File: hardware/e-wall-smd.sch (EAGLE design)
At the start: 45 parts, among them IC1 74HCT595D, IC2 74HCT595D, IC3 74HCT595D, Q1 2N7002P, Q10 2N7002P, Q11 2N7002P, Q12 2N7002P, Q13 2N7002P, Q14 2N7002P, Q15 2N7002P, Q16 2N7002P, Q17 2N7002P, Q18 2N7002P, Q19 2N7002P, Q2 2N7002P, Q20 2N7002P, Q21 2N7002P, Q22 2N7002P, Q23 2N7002P, Q24 2N7002P, Q3 2N7002P, Q4 2N7002P, Q5 2N7002P, Q6 2N7002P, Q7 2N7002P, Q8 2N7002P, Q9 2N7002P, T1 BC547, T2 BC557, T3 BC547

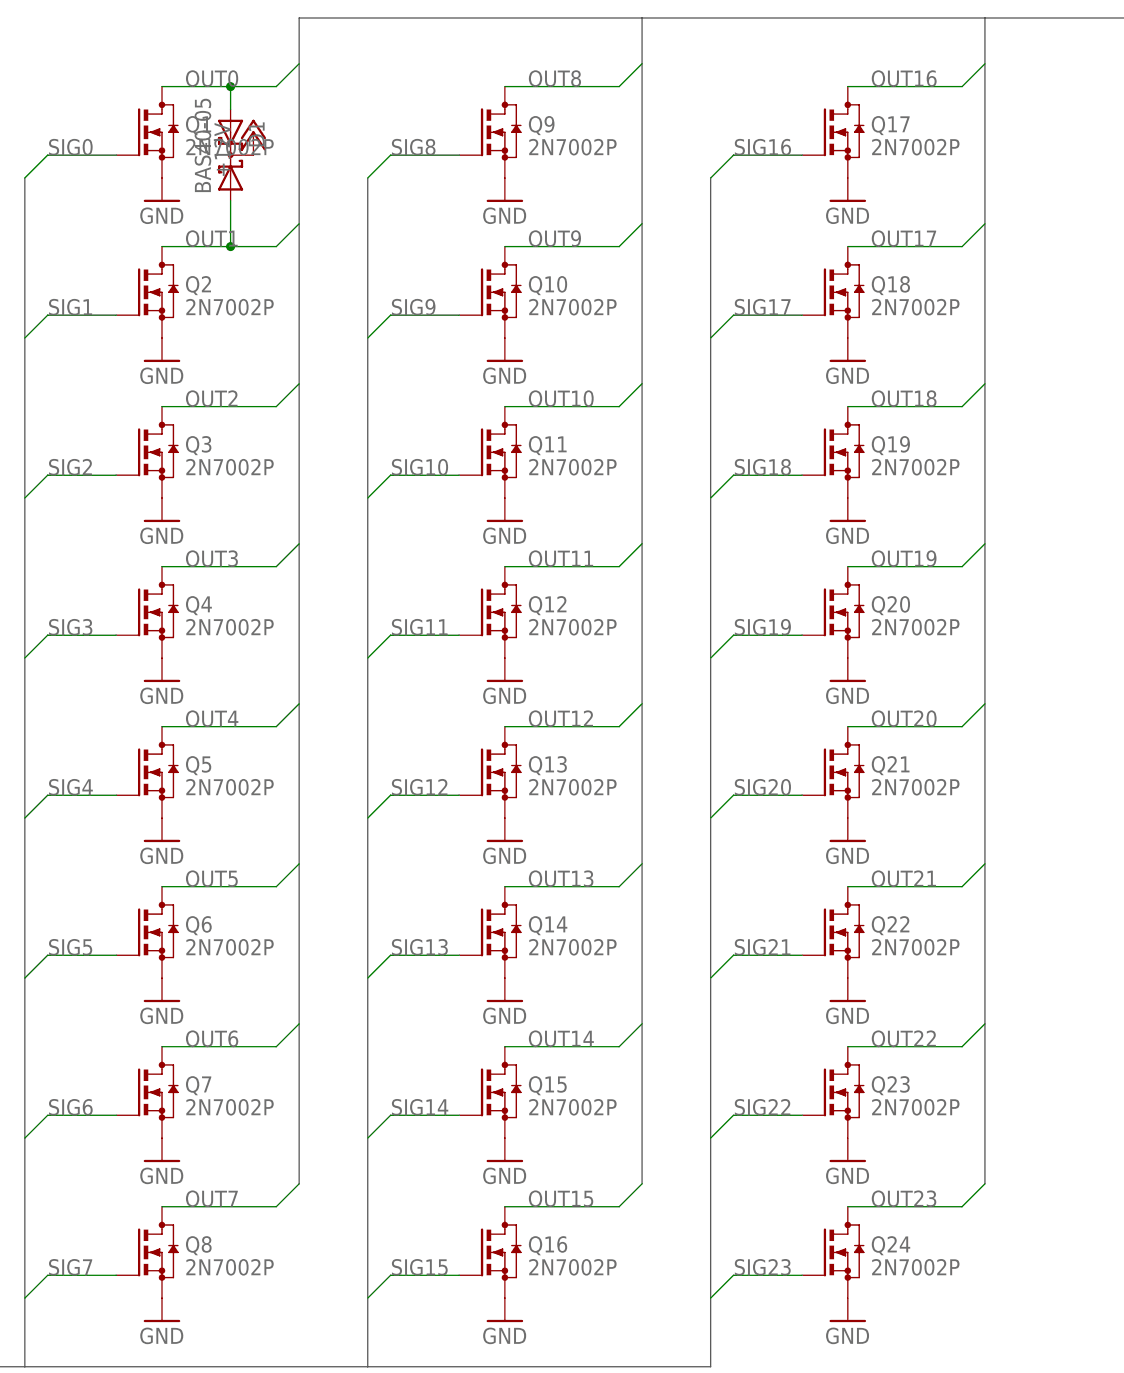
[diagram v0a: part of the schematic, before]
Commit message: Freilaufdiode ergänzt
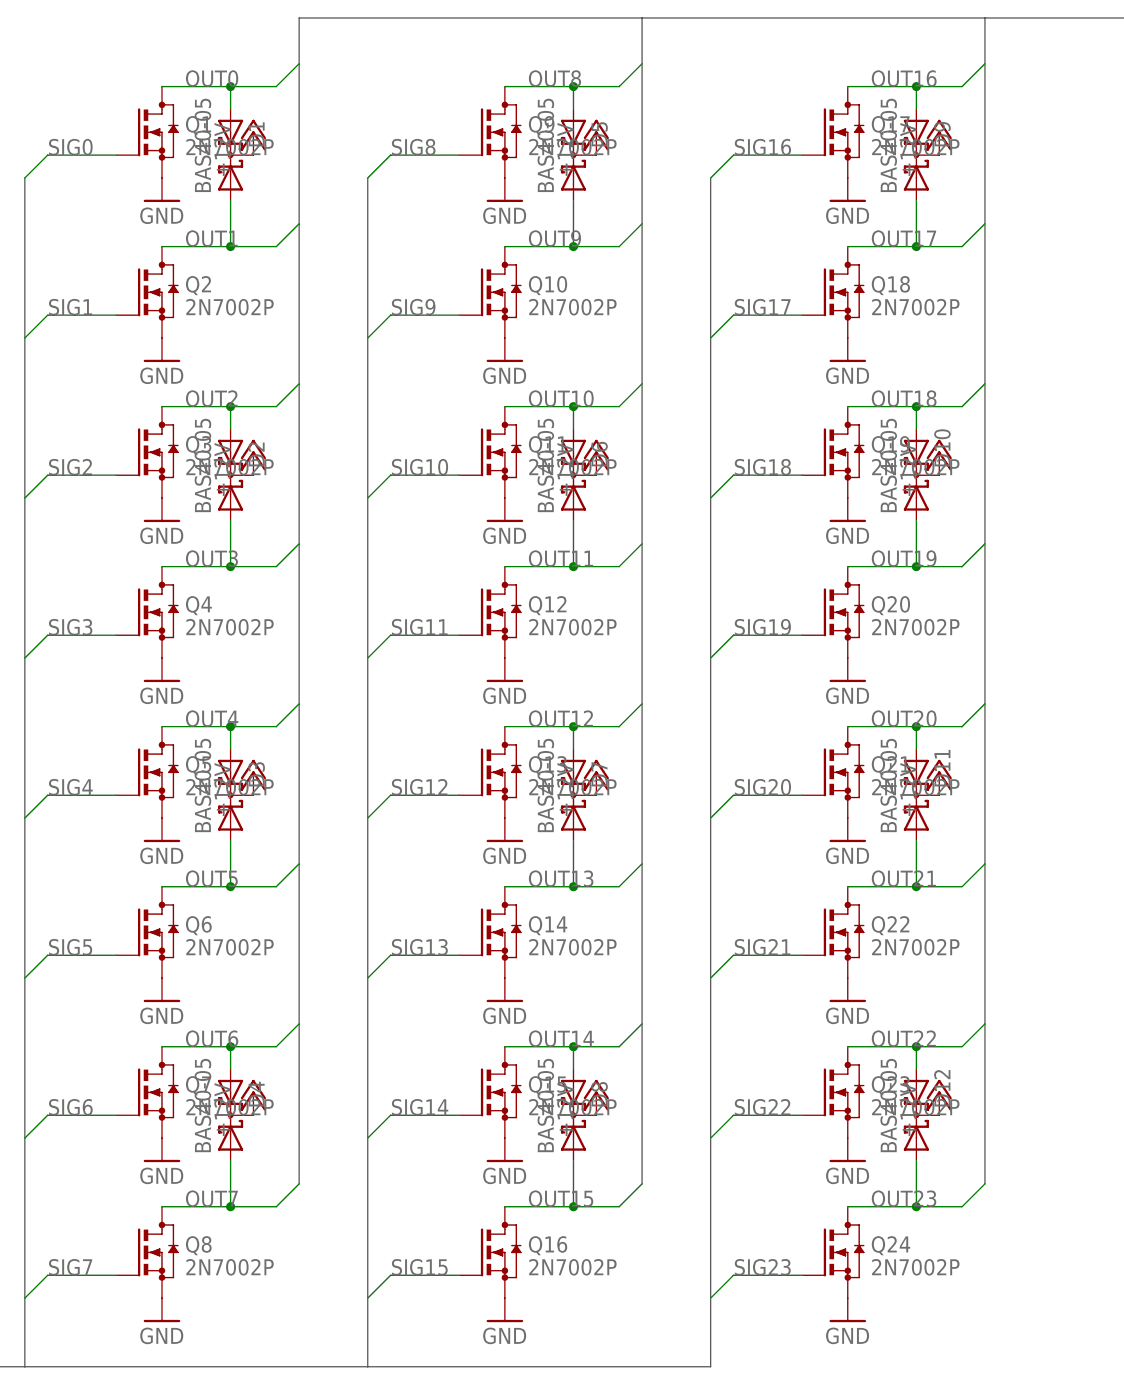
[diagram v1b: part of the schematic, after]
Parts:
- added D10, D11, D12, D2, D3, D4, D5, D6, D7, D8, D9: BAS40-05, diode:BAS40-05
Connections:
- net +12V: now also D10.C, D11.C, D12.C, D2.C, D3.C, D4.C, D5.C, D6.C, D7.C, D8.C, D9.C
- net OUT10: now also D6.A2
- net OUT11: now also D6.A1
- net OUT12: now also D7.A2
- net OUT13: now also D7.A1
- net OUT14: now also D8.A2
- net OUT15: now also D8.A1
- net OUT16: now also D9.A2
- net OUT17: now also D9.A1
- net OUT18: now also D10.A2
- net OUT19: now also D10.A1
- net OUT2: now also D2.A2
- net OUT20: now also D11.A2
- net OUT21: now also D11.A1
- net OUT22: now also D12.A2
- net OUT23: now also D12.A1
- net OUT3: now also D2.A1
- net OUT4: now also D3.A2
- net OUT5: now also D3.A1
- net OUT6: now also D4.A2
- net OUT7: now also D4.A1
- net OUT8: now also D5.A2
- net OUT9: now also D5.A1

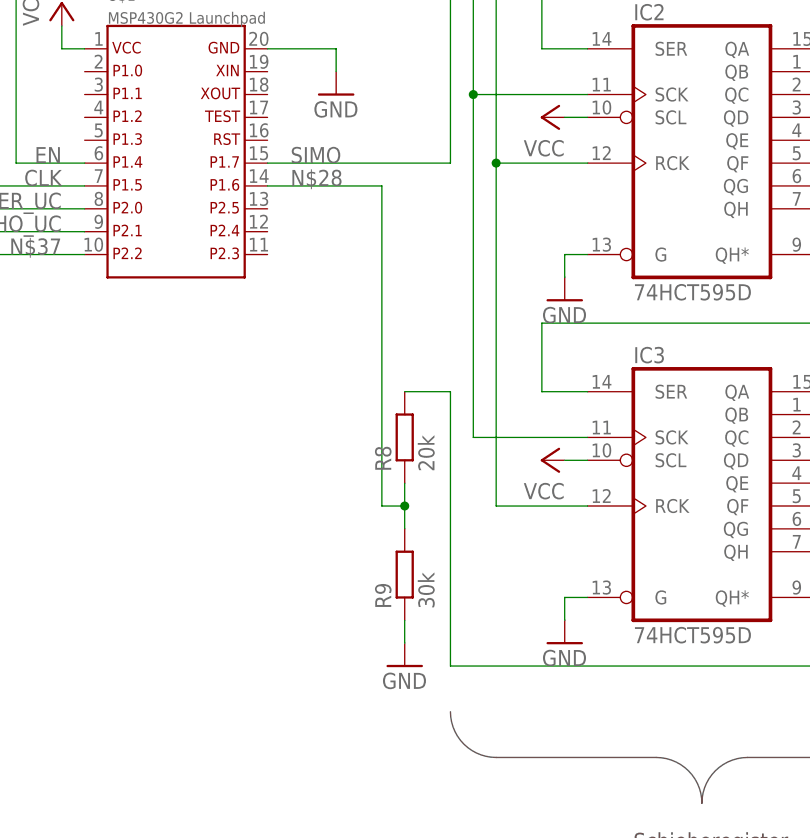
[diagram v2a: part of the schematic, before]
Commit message: Leitungen für SPI umbenannt
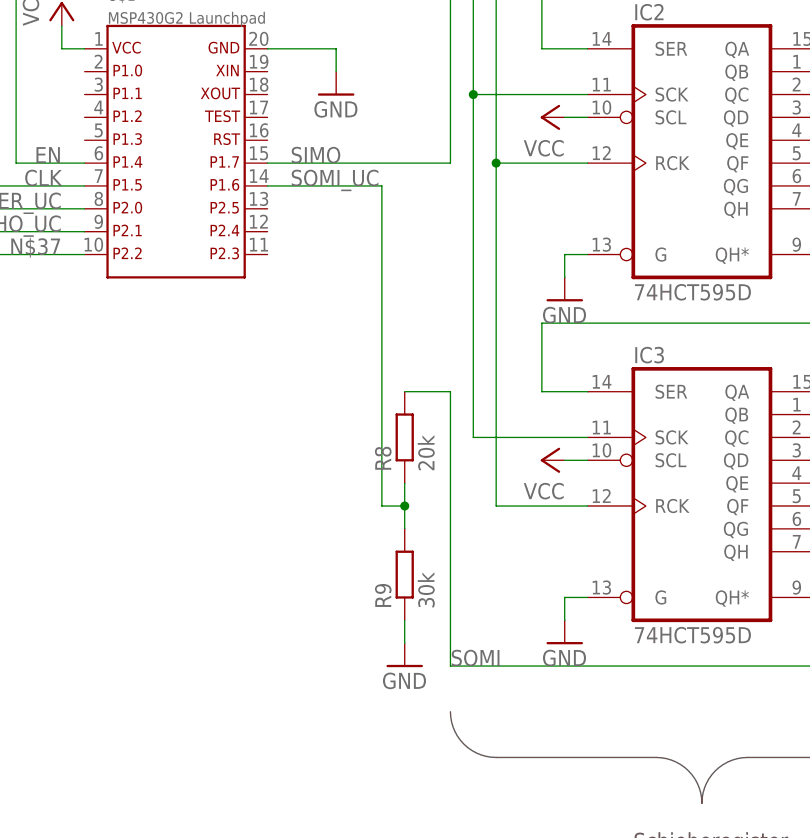
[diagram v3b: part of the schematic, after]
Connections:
- net N$28 renamed SOMI_UC
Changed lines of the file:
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@@
 <pinref part="R8" gate="G$1" pin="2"/>
 <wire x1="104.14" y1="35.56" x2="109.22" y2="35.56" width="0.1524" layer="91"/>
+<label x="109.22" y="5.08" size="1.778" layer="95"/>
 </segment>
 </net>
@@
 </segment>
 </net>
-<net name="N$28" class="0">
+<net name="SOMI_UC" class="0">
 <segment>
 <wire x1="101.6" y1="58.42" x2="88.9" y2="58.42" width="0.1524" layer="91"/>

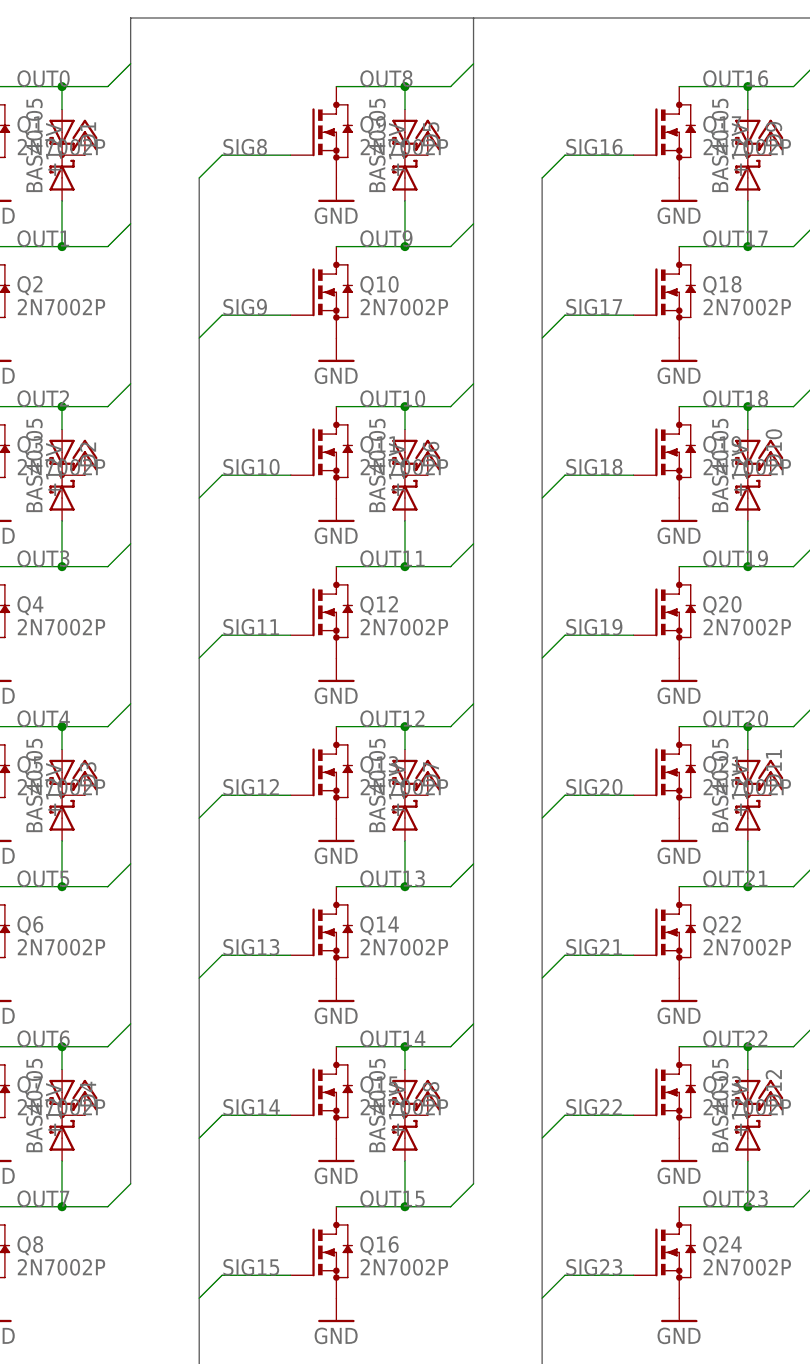
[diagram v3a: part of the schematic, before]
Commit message: Schieberegister verschoben
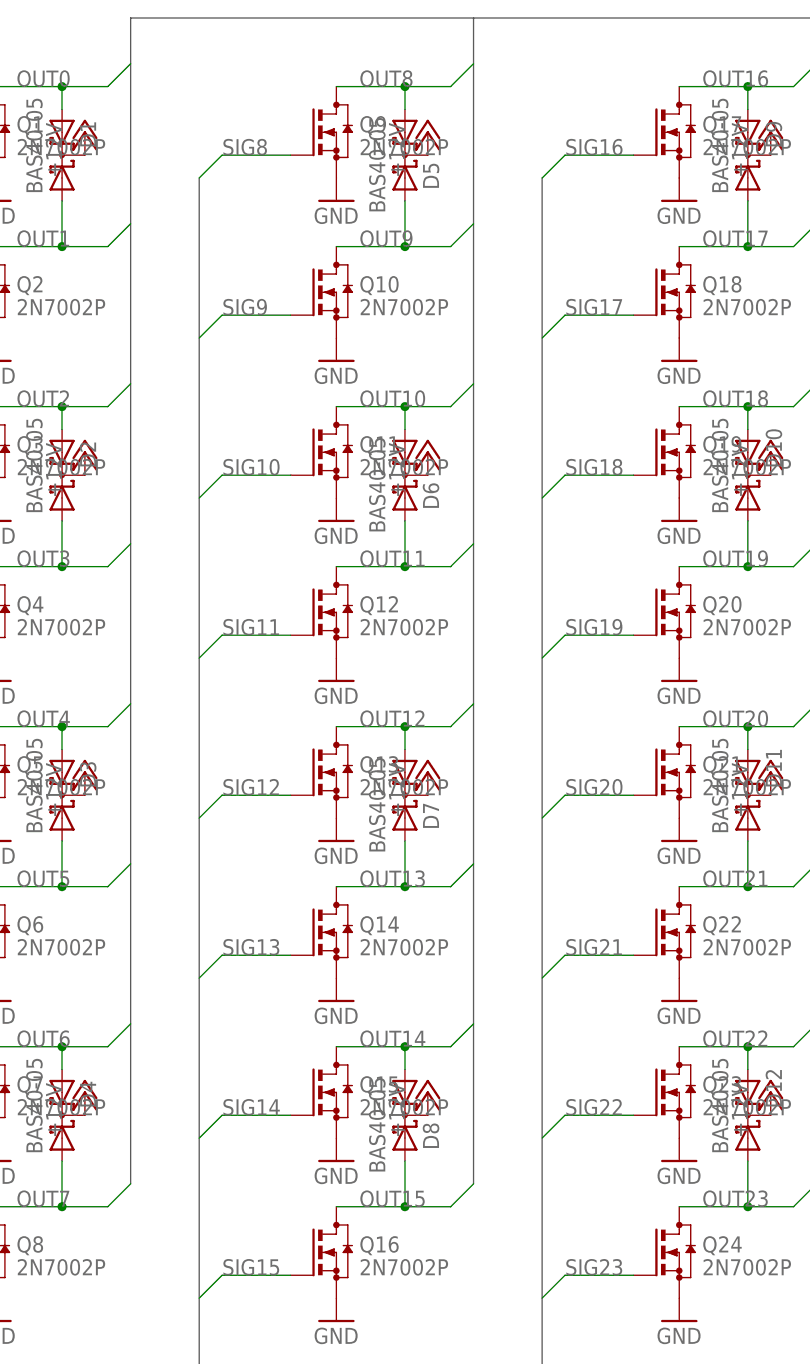
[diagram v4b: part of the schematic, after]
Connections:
- net OUT10: now also D6.A1; no longer D6.A2
- net OUT11: now also D6.A2; no longer D6.A1
- net OUT12: now also D7.A1; no longer D7.A2
- net OUT13: now also D7.A2; no longer D7.A1
- net OUT14: now also D8.A1; no longer D8.A2
- net OUT15: now also D8.A2; no longer D8.A1
- net OUT8: now also D5.A1; no longer D5.A2
- net OUT9: now also D5.A2; no longer D5.A1
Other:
- moved on the sheet: D5, D6, D7, D8
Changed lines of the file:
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@@
 <instance part="D3" gate="G$1" x="195.58" y="68.58" rot="MR90"/>
 <instance part="D4" gate="G$1" x="195.58" y="33.02" rot="MR90"/>
-<instance part="D5" gate="G$1" x="233.68" y="139.7" rot="MR90"/>
-<instance part="D6" gate="G$1" x="233.68" y="104.14" rot="MR90"/>
-<instance part="D7" gate="G$1" x="233.68" y="68.58" rot="MR90"/>
-<instance part="D8" gate="G$1" x="233.68" y="33.02" rot="MR90"/>
+<instance part="D5" gate="G$1" x="233.68" y="139.7" rot="R270"/>
+<instance part="D6" gate="G$1" x="233.68" y="104.14" rot="R270"/>
+<instance part="D7" gate="G$1" x="233.68" y="68.58" rot="R270"/>
+<instance part="D8" gate="G$1" x="233.68" y="33.02" rot="R270"/>
 <instance part="D9" gate="G$1" x="271.78" y="139.7" rot="MR90"/>
 <instance part="D10" gate="G$1" x="271.78" y="104.14" rot="MR90"/>
@@
 <wire x1="238.76" y1="147.32" x2="241.3" y2="149.86" width="0.1524" layer="91"/>
 <label x="228.6" y="147.32" size="1.778" layer="95"/>
-<pinref part="D5" gate="G$1" pin="A2"/>
+<pinref part="D5" gate="G$1" pin="A1"/>
 <wire x1="233.68" y1="144.78" x2="233.68" y2="147.32" width="0.1524" layer="91"/>
 <junction x="233.68" y="147.32"/>
@@
 <wire x1="238.76" y1="129.54" x2="241.3" y2="132.08" width="0.1524" layer="91"/>
 <label x="228.6" y="129.54" size="1.778" layer="95"/>
-<pinref part="D5" gate="G$1" pin="A1"/>
+<pinref part="D5" gate="G$1" pin="A2"/>
 <wire x1="233.68" y1="134.62" x2="233.68" y2="129.54" width="0.1524" layer="91"/>
 <junction x="233.68" y="129.54"/>
@@
 <wire x1="238.76" y1="111.76" x2="241.3" y2="114.3" width="0.1524" layer="91"/>
 <label x="228.6" y="111.76" size="1.778" layer="95"/>
-<pinref part="D6" gate="G$1" pin="A2"/>
-<wire x1="233.68" y1="109.22" x2="233.68" y2="111.76" width="0.1524" layer="91"/>
+<pinref part="D6" gate="G$1" pin="A1"/>
+<wire x1="233.68" y1="111.76" x2="233.68" y2="109.22" width="0.1524" layer="91"/>
 <junction x="233.68" y="111.76"/>
 </segment>
@@
 <wire x1="238.76" y1="93.98" x2="241.3" y2="96.52" width="0.1524" layer="91"/>
 <label x="228.6" y="93.98" size="1.778" layer="95"/>
-<pinref part="D6" gate="G$1" pin="A1"/>
-<wire x1="233.68" y1="99.06" x2="233.68" y2="93.98" width="0.1524" layer="91"/>
+<pinref part="D6" gate="G$1" pin="A2"/>
+<wire x1="233.68" y1="93.98" x2="233.68" y2="99.06" width="0.1524" layer="91"/>
 <junction x="233.68" y="93.98"/>
 </segment>
@@
 <wire x1="238.76" y1="76.2" x2="241.3" y2="78.74" width="0.1524" layer="91"/>
 <label x="228.6" y="76.2" size="1.778" layer="95"/>
-<pinref part="D7" gate="G$1" pin="A2"/>
+<pinref part="D7" gate="G$1" pin="A1"/>
 <wire x1="233.68" y1="73.66" x2="233.68" y2="76.2" width="0.1524" layer="91"/>
 <junction x="233.68" y="76.2"/>
@@
 <wire x1="238.76" y1="58.42" x2="241.3" y2="60.96" width="0.1524" layer="91"/>
 <label x="228.6" y="58.42" size="1.778" layer="95"/>
-<pinref part="D7" gate="G$1" pin="A1"/>
+<pinref part="D7" gate="G$1" pin="A2"/>
 <wire x1="233.68" y1="63.5" x2="233.68" y2="58.42" width="0.1524" layer="91"/>
 <junction x="233.68" y="58.42"/>
@@
 <wire x1="238.76" y1="40.64" x2="241.3" y2="43.18" width="0.1524" layer="91"/>
 <label x="228.6" y="40.64" size="1.778" layer="95"/>
-<pinref part="D8" gate="G$1" pin="A2"/>
-<wire x1="233.68" y1="40.64" x2="233.68" y2="38.1" width="0.1524" layer="91"/>
+<pinref part="D8" gate="G$1" pin="A1"/>
+<wire x1="233.68" y1="38.1" x2="233.68" y2="40.64" width="0.1524" layer="91"/>
 <junction x="233.68" y="40.64"/>
 </segment>
@@
 <wire x1="238.76" y1="22.86" x2="241.3" y2="25.4" width="0.1524" layer="91"/>
 <label x="228.6" y="22.86" size="1.778" layer="95"/>
-<pinref part="D8" gate="G$1" pin="A1"/>
+<pinref part="D8" gate="G$1" pin="A2"/>
 <wire x1="233.68" y1="27.94" x2="233.68" y2="22.86" width="0.1524" layer="91"/>
 <junction x="233.68" y="22.86"/>
